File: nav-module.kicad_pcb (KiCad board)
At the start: 4 copper layers, 100 x 100 mm, 207 parts, among them J1100 Conn_Coaxial, J200 09031967921, J800 USB_C_Receptacle_USB2.0_16P, Q700 MMST3904, SW400 TL2243, U100 W25Q128, U1100 ZED-F9P, U1200 BNO055, U200 PESD5V0S2BT, U300 TPS563201DDCR, U301 TPS563201DDCR, U302 CH334P, U400 STM32H750VBTx, U500 TJA1044GTK_3Z, U600 TJA1044GTK_3Z, U700 STM32F103CBTx, U801 FSUSB42UMX, U802 PESD5V0S2BT, X1200 Q13FC1350000400, X300 Q13FC1350000400, X400 X322512MSB4SI, Y700 8 MHz, Y900 12Mhz

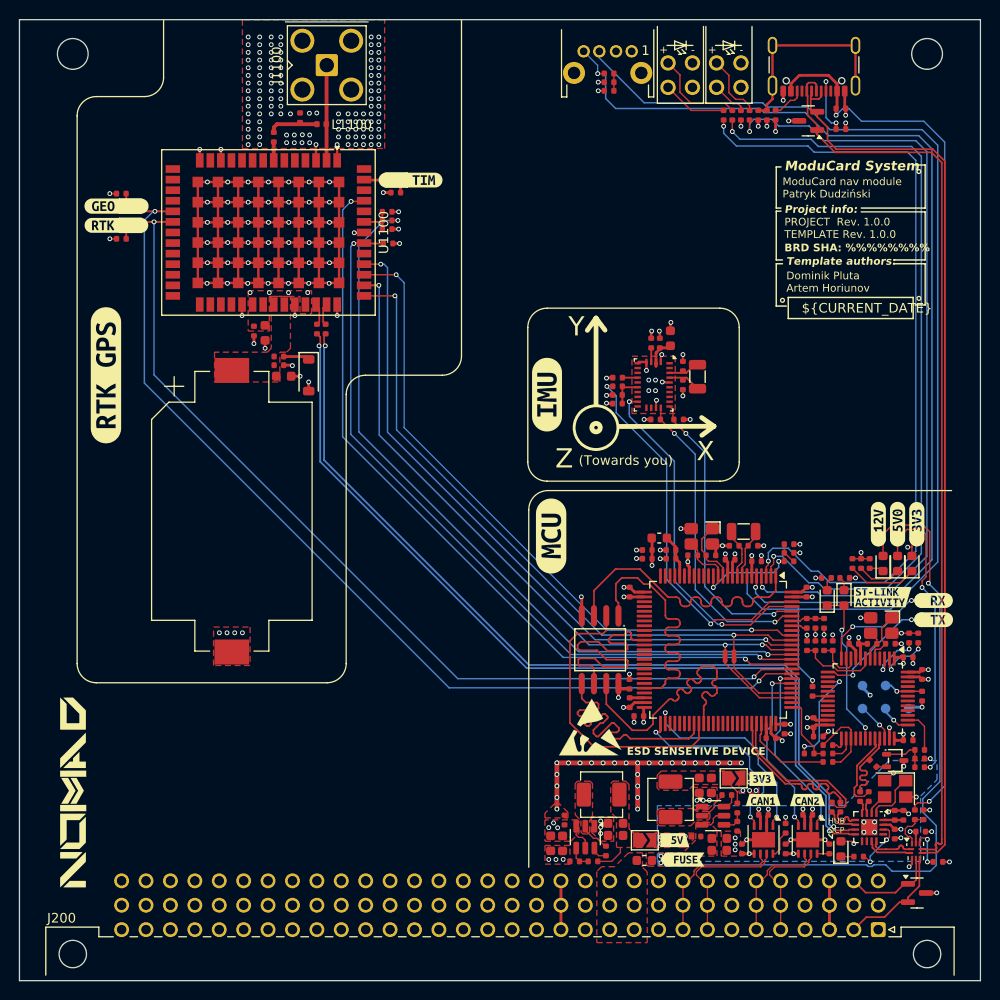
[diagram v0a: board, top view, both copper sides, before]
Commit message: [barometer] added presure sensor
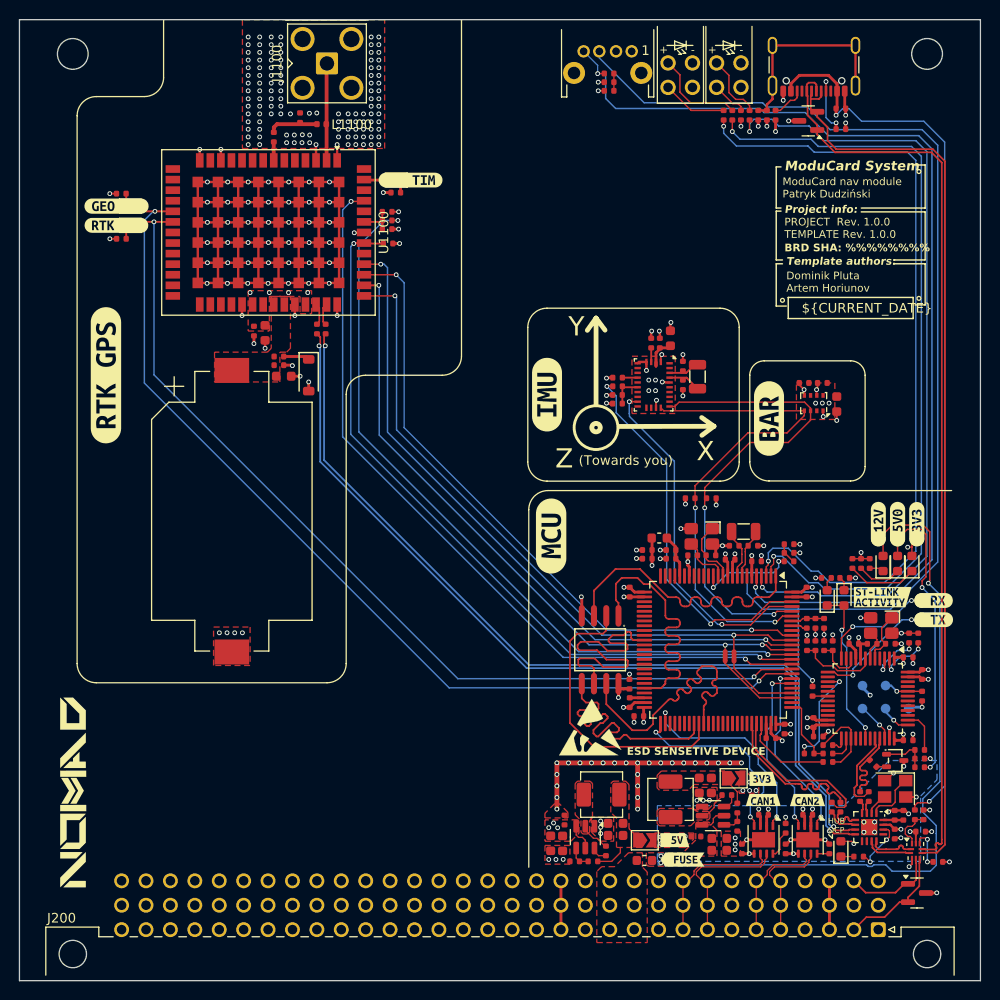
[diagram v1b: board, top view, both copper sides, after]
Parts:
- added C1300: 10uF, PCM_JLCPCB:C_0603, F.Cu at (124.4, 91.3)
- added C1301: 100nF, PCM_JLCPCB:C_0402, F.Cu at (122.9, 89.1)
- added C1302: 100nF, PCM_JLCPCB:C_0402, F.Cu at (121.0, 89.1)
- added U1300: BMP280, Package_LGA:Bosch_LGA-8_2x2.5mm_P0.65mm_ClockwisePinNumbering, F.Cu at (122.0, 91.2)
- added kibuzzard-67BE5A95: G***, kibuzzard-67BE5A95, F.Cu at (117.4, 92.8)
- moved R426 8.96 mm to (109.2, 101.1)
- moved R427 8.88 mm to (111.4, 101.1)
- moved J1100 0.18 mm to (71.4, 55.8)
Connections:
- net /IMU/IMU_I2C.SCL renamed /Barometr/BAROMETR_I2C.SCL
- net /IMU/IMU_I2C.SDA renamed /Barometr/BAROMETR_I2C.SDA
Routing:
- net /Barometr/BAROMETR_I2C.SCL: track 32.1 -> 52.5 mm
- net /Barometr/BAROMETR_I2C.SDA: track 30.7 -> 51.0 mm
- net GND: track 317.7 -> 322.1 mm, vias 285 -> 289
- net +3V3: track 52.4 -> 52.3 mm, vias 44 -> 47
